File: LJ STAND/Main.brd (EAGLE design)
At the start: 180 x 152 mm, 213 parts, among them Q1 200mA/50V

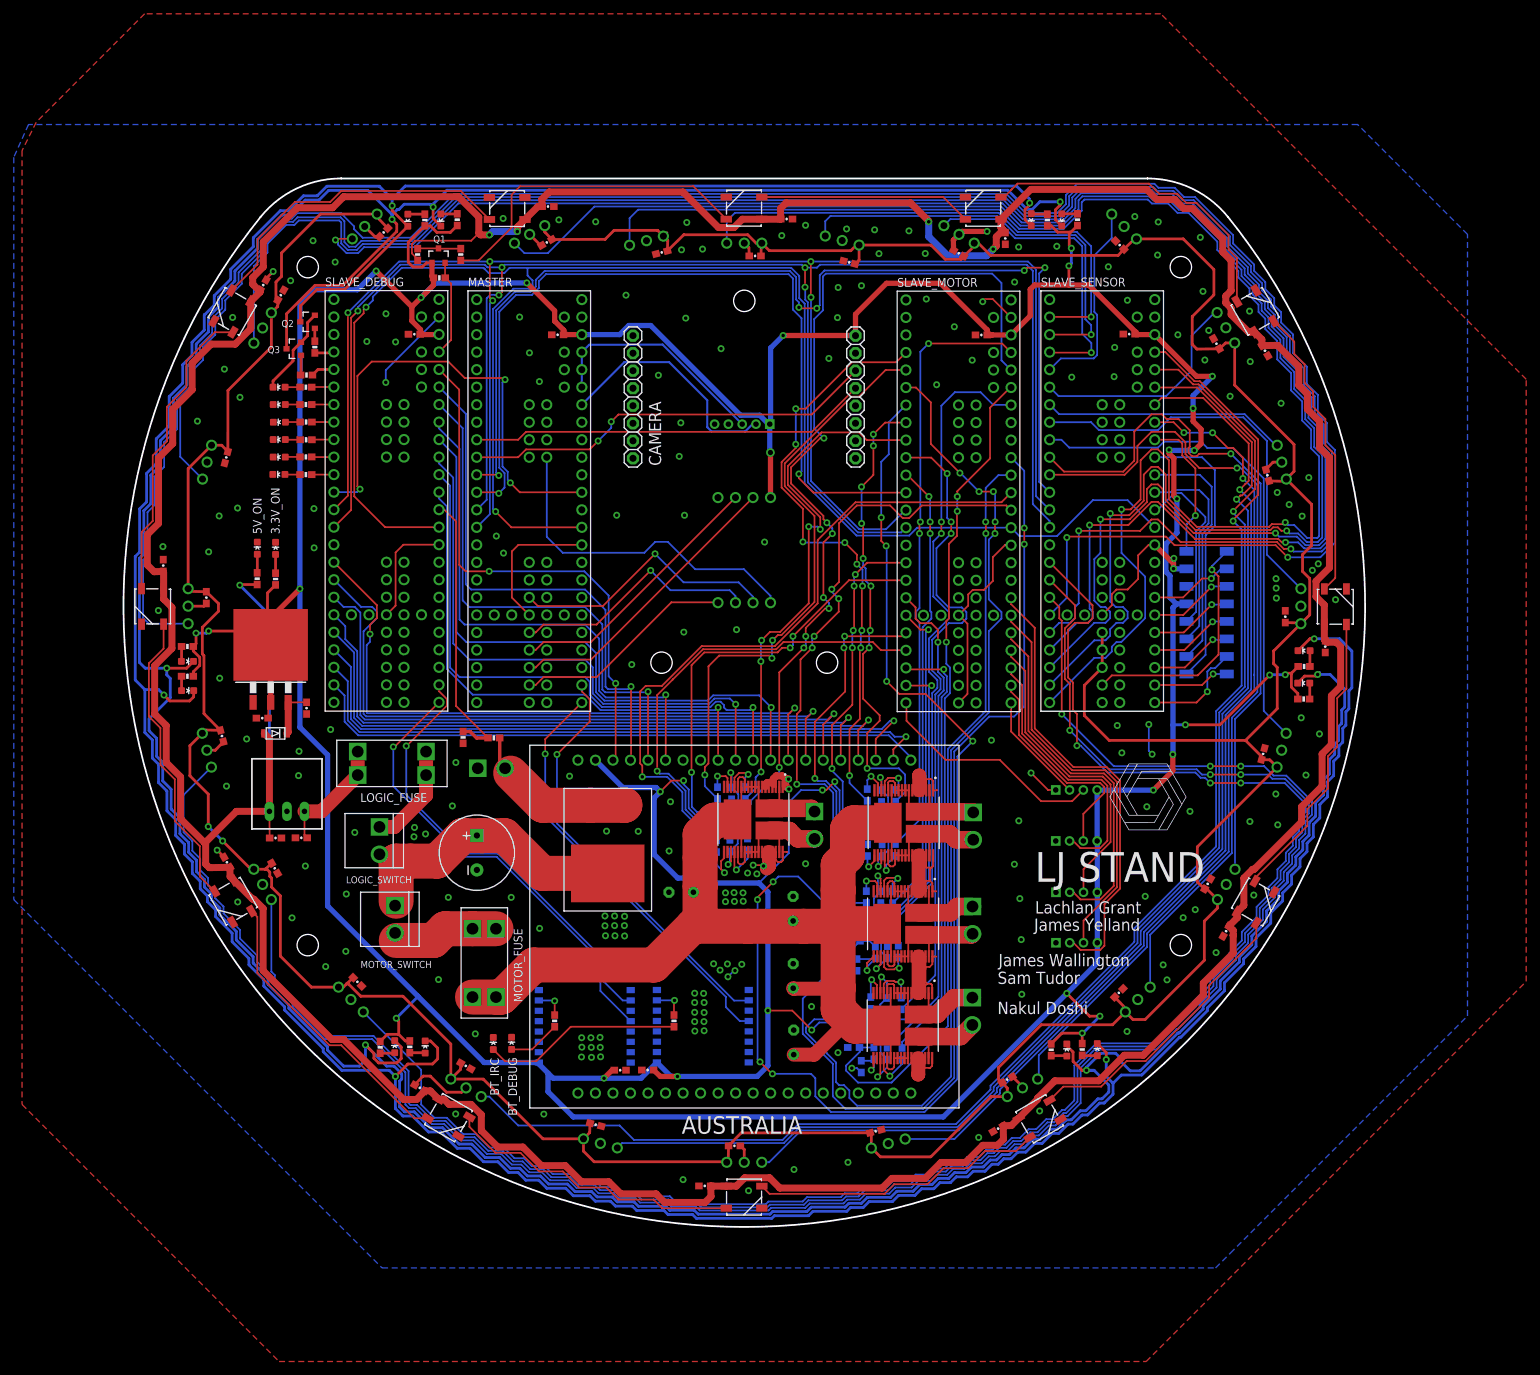
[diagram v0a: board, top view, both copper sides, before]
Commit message: Pin changes on teensys, removed some screen pins for motor grounding
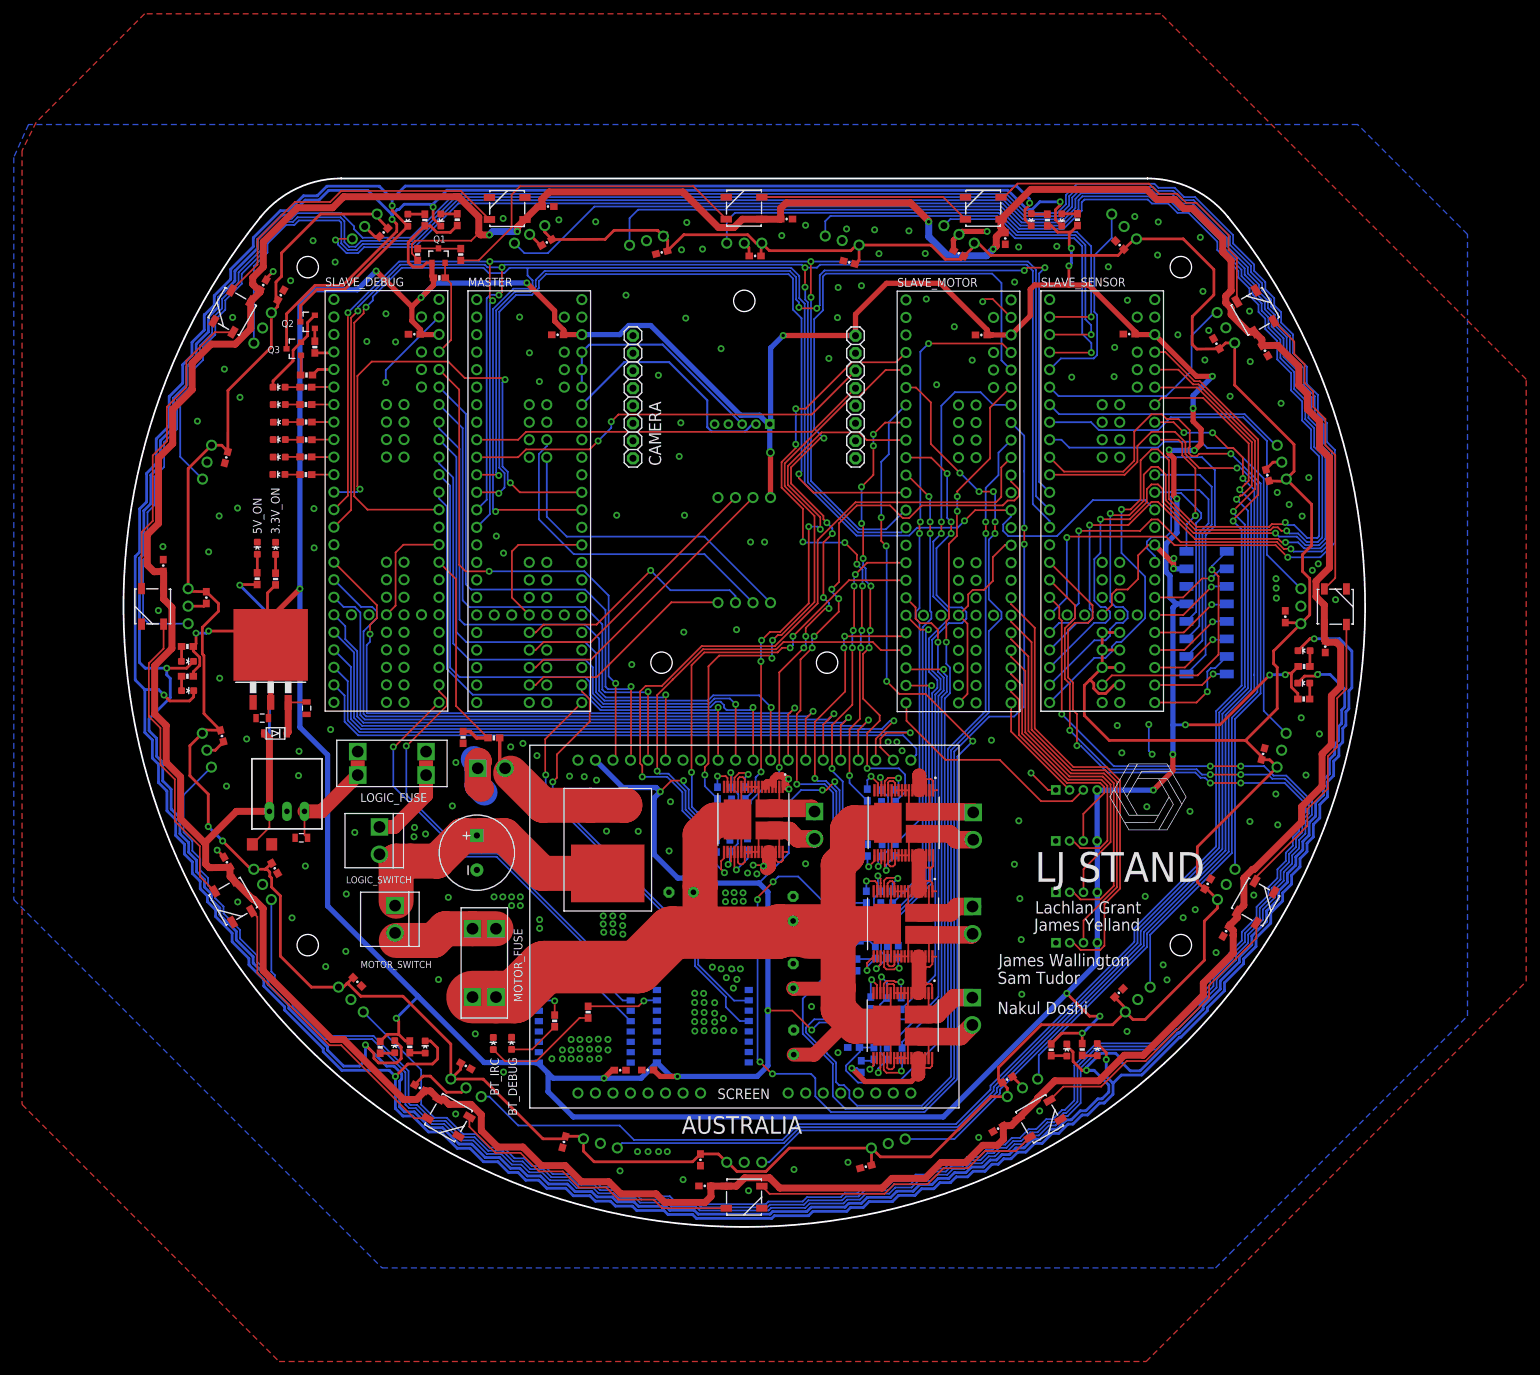
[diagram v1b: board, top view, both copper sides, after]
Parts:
- C2, C4, C5: device SparkFun-Capacitors:0603-CAP -> SparkFun-Capacitors:0805
- C3: device SparkFun-Capacitors:0603-CAP -> SparkFun-Capacitors:1206
- moved R5 12.5 mm to (67.4, 31.1)
- moved C50 5.33 mm to (83.6, 9.73), turned to 270 degrees
- moved C49 5.32 mm to (107.6, 8.74), turned to 195 degrees
- moved C51 5.24 mm to (63.9, 12.3), turned to 255 degrees
- moved C3 2.17 mm to (20.1, 55.5)
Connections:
- net GND: now also SCREEN.GND
- net GYRO_CS2: now also MASTER.55; no longer MASTER.42
- net IR_PWR: now also SLAVE_SENSOR.47, SLAVE_SENSOR.48, SLAVE_SENSOR.49, SLAVE_SENSOR.50
- net LS0: now also SLAVE_SENSOR.DA1; no longer SLAVE_SENSOR.14
- net MOTOR1_CS: now also SLAVE_MOTOR.16; no longer SLAVE_MOTOR.14
- net MOTOR2_CS: now also SLAVE_MOTOR.17; no longer SLAVE_MOTOR.15
- net MOTOR3_CS: now also SLAVE_MOTOR.18; no longer SLAVE_MOTOR.16
- net MOTOR4_CS: now also SLAVE_MOTOR.19; no longer SLAVE_MOTOR.17
- net SCK: now also MASTER.14, SLAVE_DEBUG.14, SLAVE_MOTOR.14, SLAVE_SENSOR.14; no longer MASTER.13, SLAVE_DEBUG.13, SLAVE_MOTOR.13, SLAVE_SENSOR.13
- net V_BAT: now also SLAVE_DEBUG.DA1; no longer SLAVE_DEBUG.14
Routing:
- net GND: track 255.1 -> 271.8 mm, vias 202 -> 240
- net MOTOR_PWR: track 191.1 -> 206.3 mm
- net N$17: track 29.0 -> 17.0 mm
- net IR_PWR: track 615.1 -> 627.0 mm
- net LS0: track 26.1 -> 35.0 mm
- net GYRO_CS2: track 39.5 -> 48.1 mm, vias 1 -> 0
- net V_BAT: track 40.9 -> 32.8 mm
- net N$18: track 4.71 -> 10.3 mm
- net MOTOR4_CS: track 147.5 -> 152.6 mm
- net MOTOR1_CS: track 92.9 -> 97.8 mm
- net SCREEN_D6: track 94.6 -> 99.4 mm
- net MOTOR2_CS: track 100.4 -> 105.0 mm
- net MOTOR3_CS: track 109.9 -> 114.5 mm
- net GYRO_CS3: track 49.8 -> 46.2 mm
- net SCK: track 250.9 -> 253.4 mm, vias 2 -> 3
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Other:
- board text added: "SCREEN"

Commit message: Small fixes incl. grounding
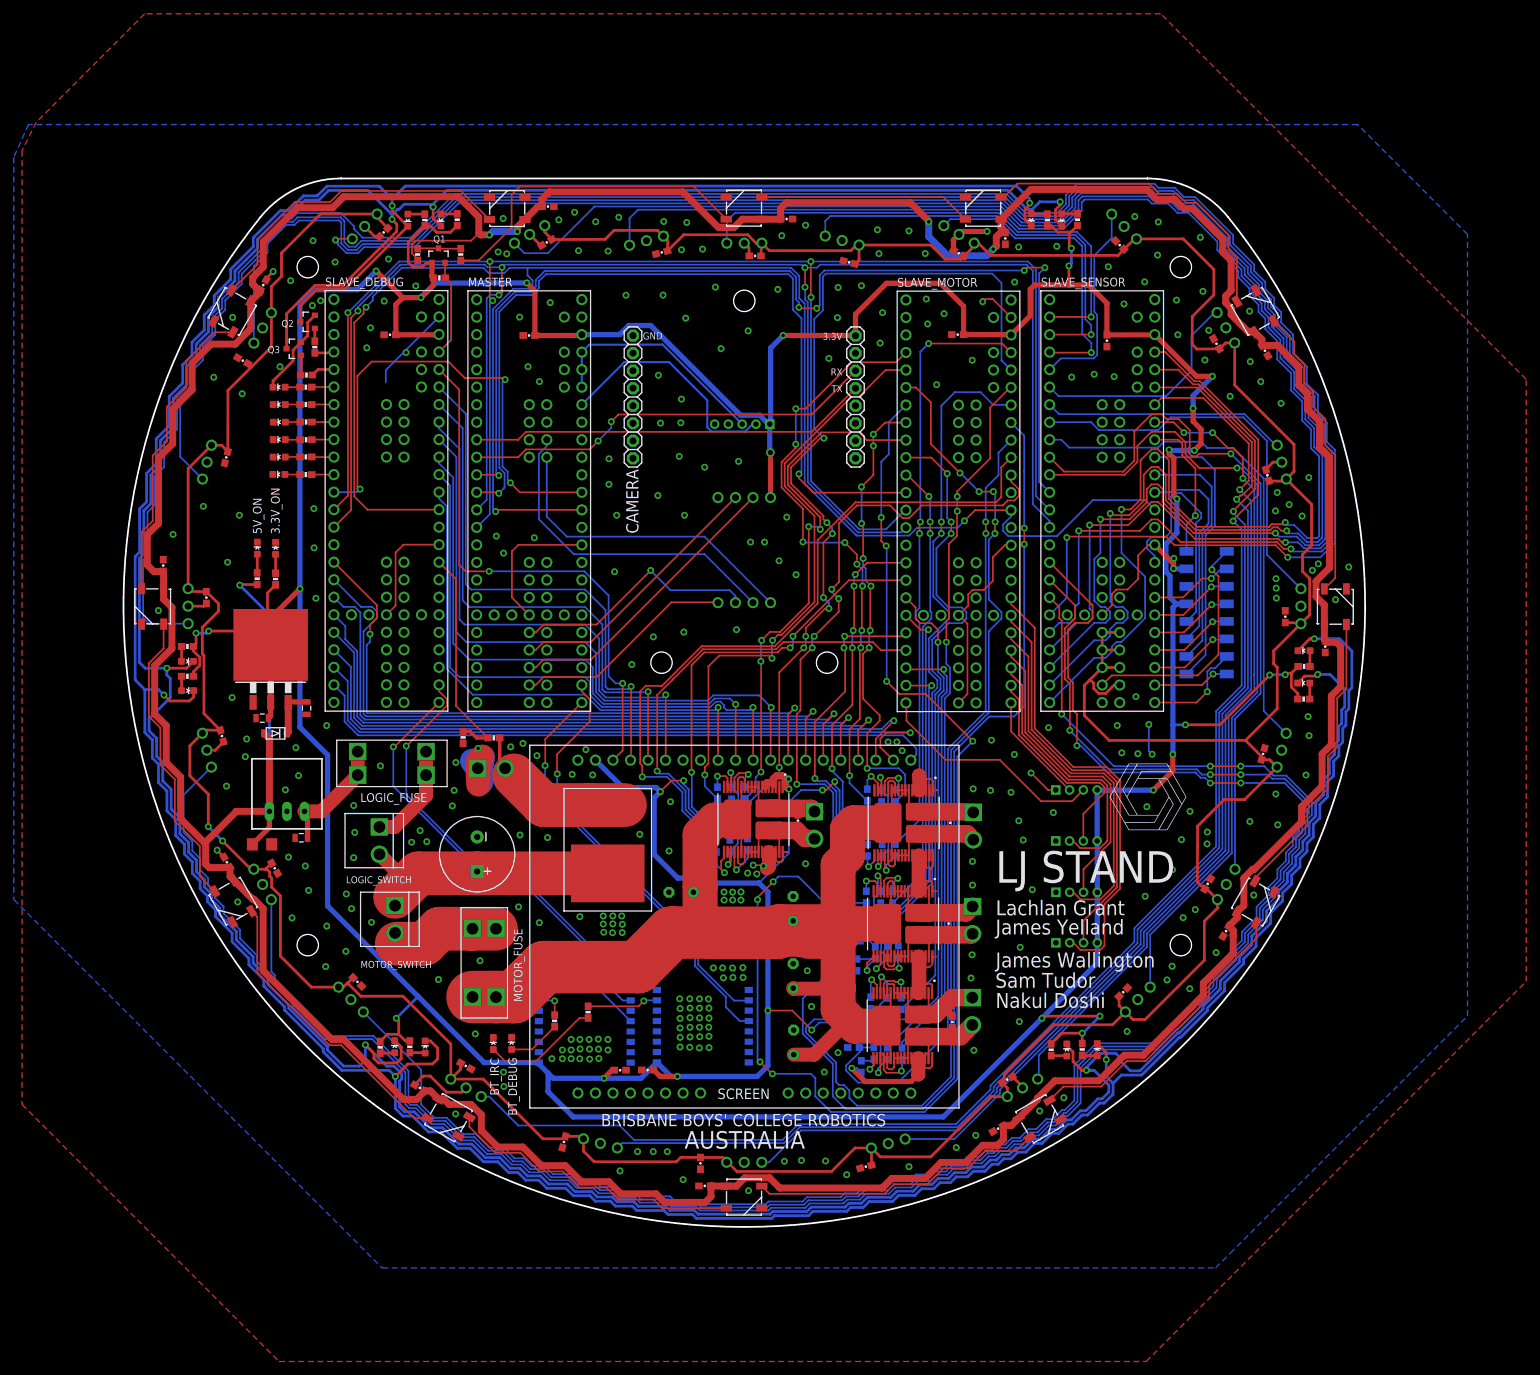
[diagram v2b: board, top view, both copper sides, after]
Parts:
- added C20, C21, C22, C23: 0.1uF, SparkFun-Capacitors:0603-CAP
- moved C58 11.0 mm to (17.3, 125.6), turned to 150 degrees
- moved C16 4.14 mm to (58.8, 129.2)
- moved C14 3.53 mm to (38.6, 129.3)
- moved C17 3.43 mm to (120.9, 129.4)
- moved C15 3.37 mm to (142.6, 128.5), turned to 270 degrees
- moved C47 0.64 mm to (144.9, 34.0)
- moved C50 0.51 mm to (83.6, 9.22)
- moved C1 0.23 mm to (51.3, 54.0), turned to 270 degrees
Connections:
- net MOTOR1_OUTA: now also C20.1
- net MOTOR1_OUTB: now also C20.2
- net MOTOR2_OUTA: now also C21.1
- net MOTOR2_OUTB: now also C21.2
- net MOTOR3_OUTA: now also C23.1
- net MOTOR3_OUTB: now also C23.2
- net MOTOR4_OUTA: now also C22.1
- net MOTOR4_OUTB: now also C22.2
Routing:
- net 3.3V: track 855.8 -> 869.3 mm
- net N$12: track 45.4 -> 40.6 mm
- net MOTOR3_OUTA: track 21.9 -> 25.2 mm
- net GND: track 271.8 -> 274.4 mm, vias 240 -> 318
- net MOTOR1_OUTB: track 22.1 -> 24.3 mm
- net SCREEN_CS: track 77.5 -> 79.5 mm
- net MOTOR2_OUTA: track 21.4 -> 22.5 mm
- net MOTOR1_OUTA: track 22.6 -> 23.6 mm
- net MOTOR4_OUTB: track 21.3 -> 22.2 mm
- net N$1: track 16.3 -> 17.1 mm
- net MOTOR2_OUTB: track 22.4 -> 21.6 mm
- net MOTOR4_OUTA: track 22.8 -> 23.5 mm
- net BT_IRC_RX: track 61.5 -> 61.0 mm
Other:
- board text added: "BRISBANE BOYS' COLLEGE ROBOTICS"
- board text added: "RX"
- board text added: "TX"

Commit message: Final changes to main
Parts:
- VREG-3.3: value (none) -> LM340S-05
- moved R2 1.89 mm to (48.3, 72.6), turned to 180 degrees
- moved LOGIC_FUSE 1.47 mm to (45.3, 69.0)
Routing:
- net N$13: track 17.3 -> 18.8 mm
- net MOTOR2_ENCA: track 32.2 -> 33.2 mm

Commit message: Final main + gerbers
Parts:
- C1: device SparkFun-Capacitors:CPOL-RADIAL-1000UF-25V-KIT -> SparkFun-Capacitors:CPOL-RADIAL-1000UF-25V
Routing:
- net GND: track 274.4 -> 278.8 mm
